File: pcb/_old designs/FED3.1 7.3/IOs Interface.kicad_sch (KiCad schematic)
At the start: 29 parts, among them IC1 MC74VHC1GT125, Q2 DMP2035U-7

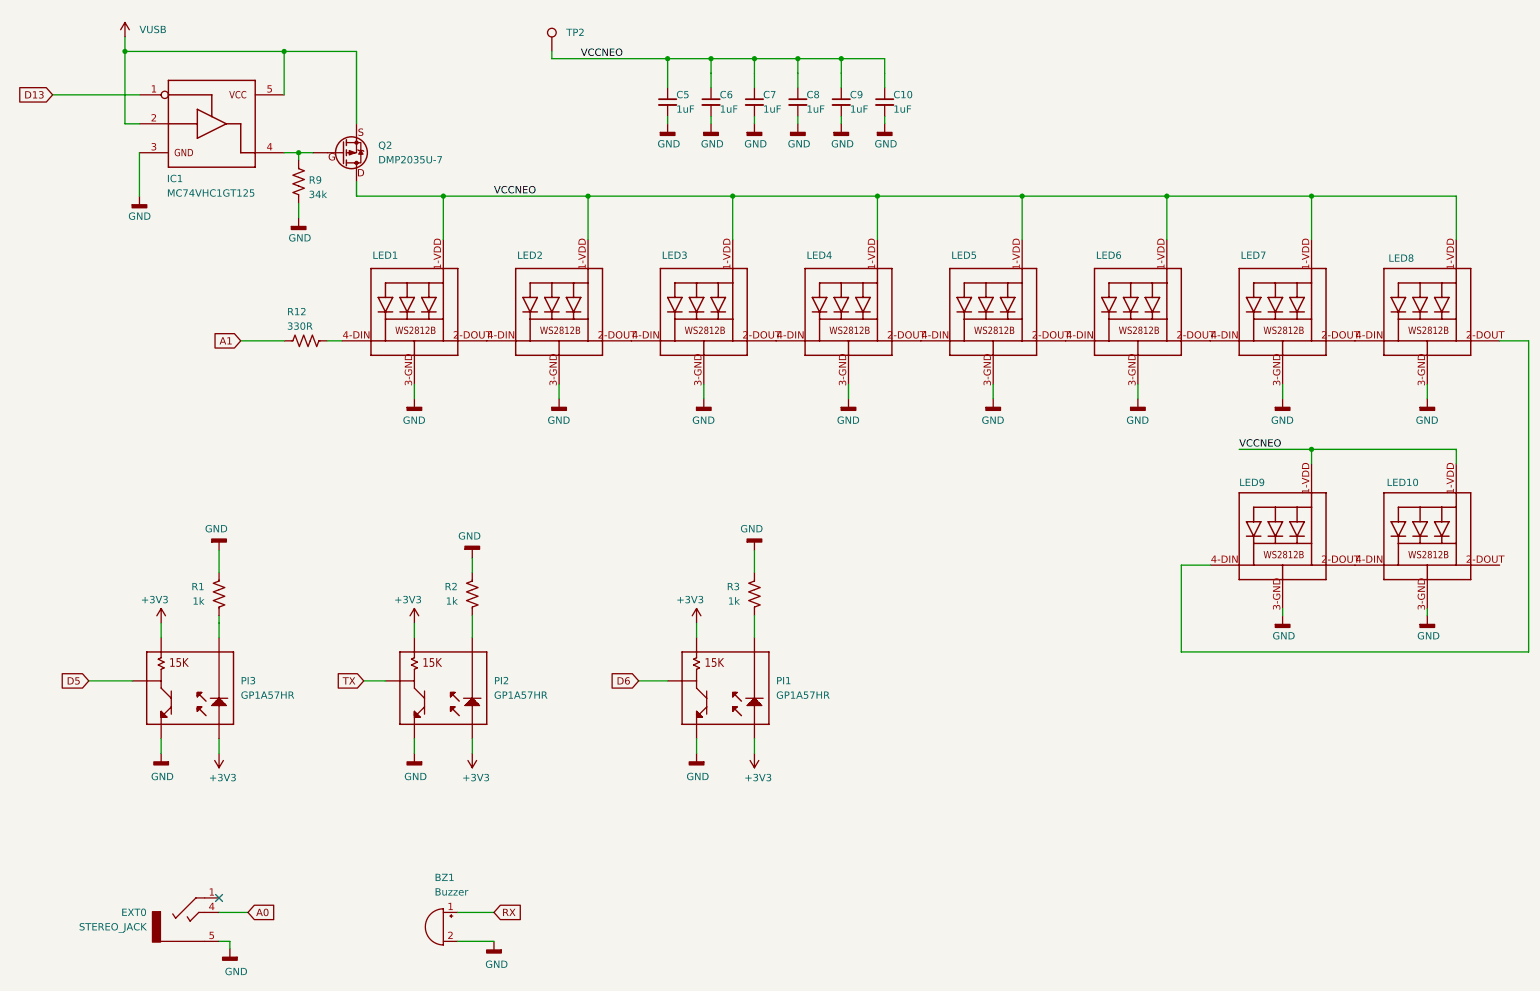
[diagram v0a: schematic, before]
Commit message: v.7.4 - alterações rail power
v.7.4
- modificada estrutura rail power: VUSB apenas para Vcharging
- modificadas Rs de LEDs para diminuir I
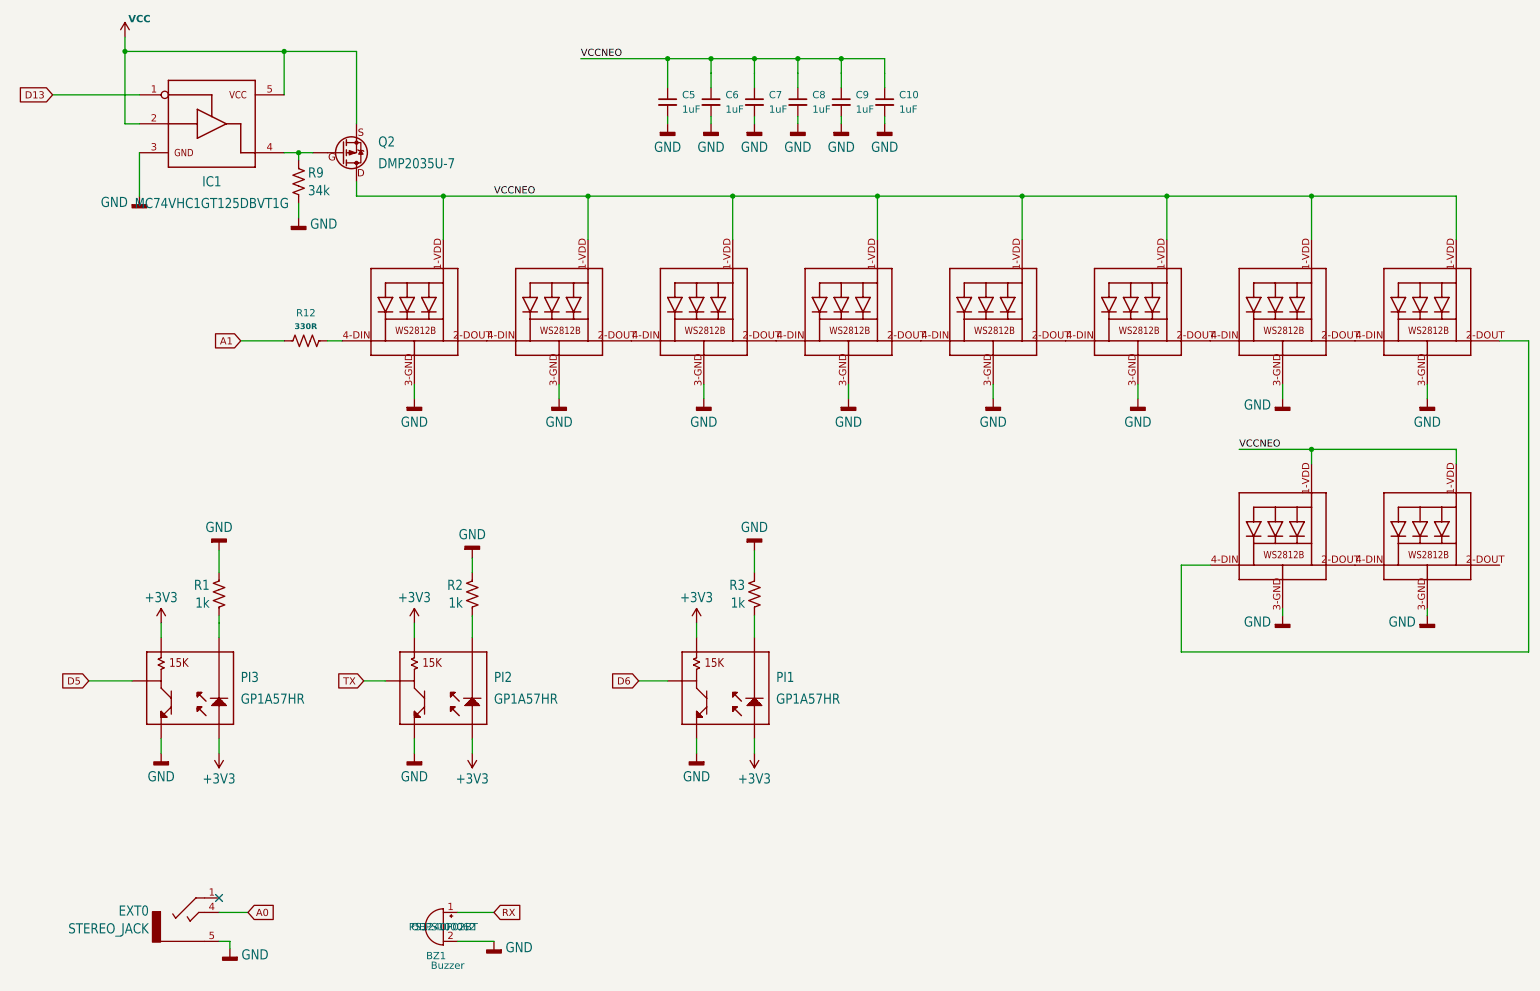
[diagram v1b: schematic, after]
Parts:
- removed TP2: VccNEO, TestPoint:TestPoint_Pad_1.0x1.0mm, symbol Connector:TestPoint
- BZ1: footprint FED3_PCBLib:Buzzer -> FED3_v7.3:Buzzer
- EXT0: footprint FED3_PCBLib:35RASMT2BHNTRX -> FED3_v7.3:35RASMT2BHNTRX; symbol FED3 SymbLib:STEREO_JACK -> FED3_v7.3 SymLib:STEREO_JACK
- IC1: value MC74VHC1GT125 -> MC74VHC1GT125DBVT1G; symbol FED3 SymbLib:SN74LVC1G125 -> FED3_v7.3 SymLib:SN74LVC1G125
- LED1, LED10, LED2, LED3, LED4, LED5, LED6, LED7, LED8, LED9: footprint FED3_PCBLib:WS2812B -> FED3_v7.3:WS2812B; symbol FED3 SymbLib:WS2812B5050 -> FED3_v7.3 SymLib:WS2812B5050; MPN SK6812RGBW-BW -> XT1511RGBW-BW
- PI1, PI2, PI3: footprint FED3_PCBLib:GP1A57HR -> FED3_v7.3:GP1A57HR; symbol FED3 SymbLib:GP1A57HR -> FED3_v7.3 SymLib:GP1A57HR
- Q2: footprint FED3_PCBLib:TSMT3 -> FED3_v7.3:TSMT3; symbol FED3 SymbLib:MOSFET_P-CH -> FED3_v7.3 SymLib:MOSFET_P-CH
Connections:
- net VUSB renamed VCC
